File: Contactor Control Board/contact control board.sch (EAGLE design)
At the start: 35 parts, among them Q1 2n2222, Q2 2n2222, Q3 2n2222, Q4 MOSFET-NCHANNELFQP30N06L

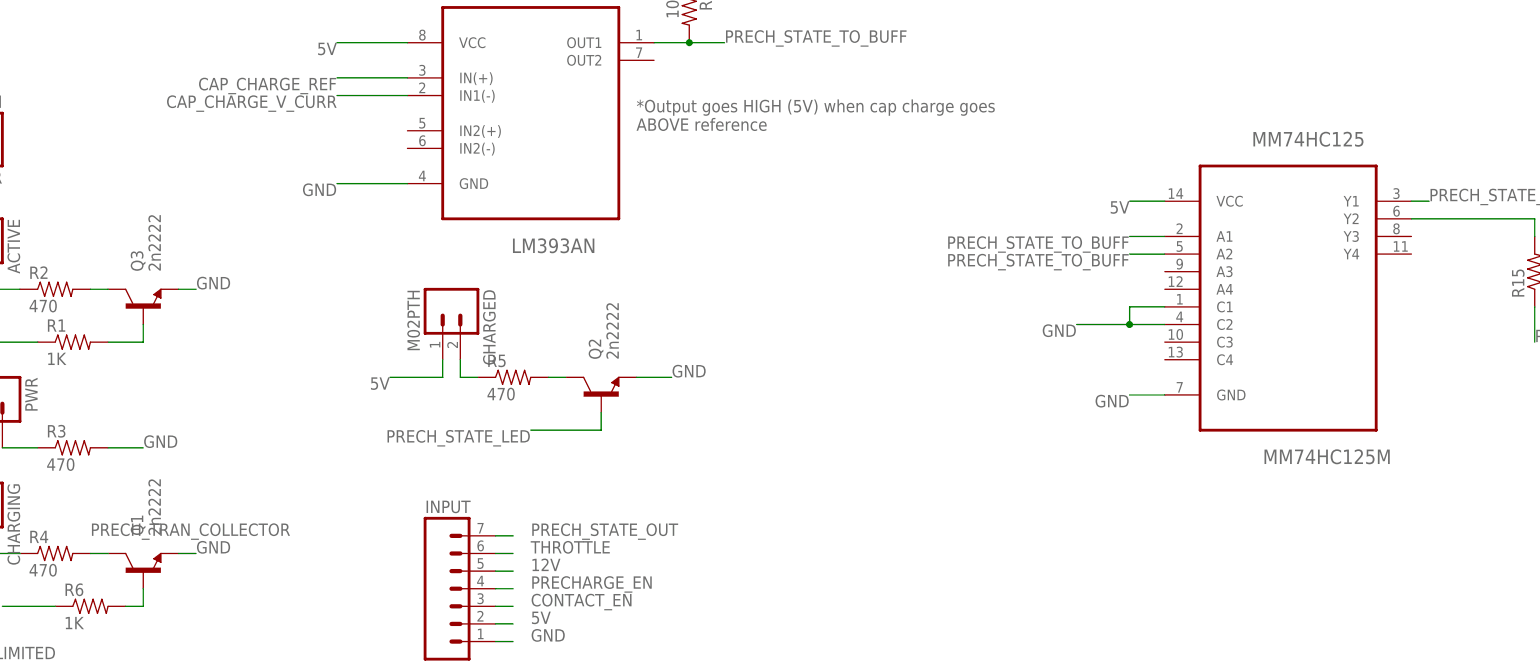
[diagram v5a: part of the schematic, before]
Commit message: Using the proper chip package for the buffer chip
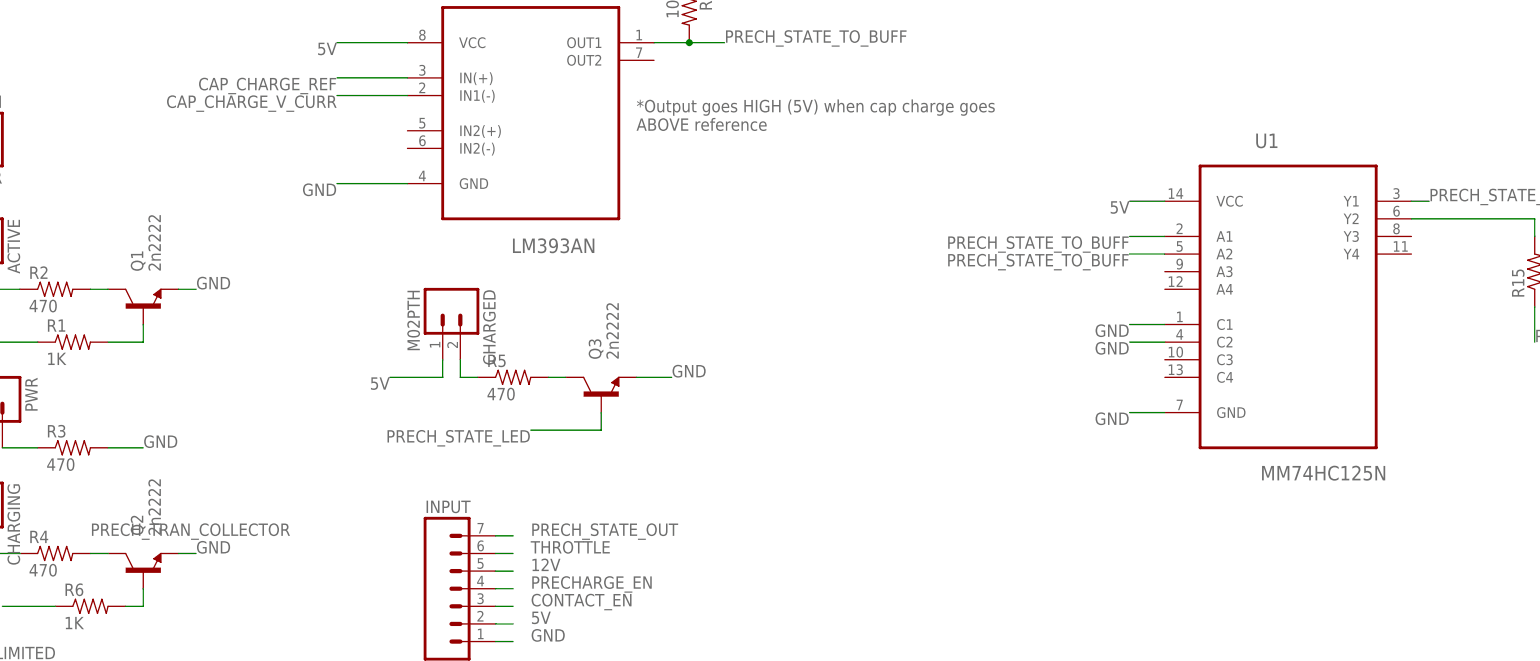
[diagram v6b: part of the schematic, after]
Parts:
- removed MM74HC125: MM74HC125M, Fairchild_By_element14_Batch_1:MM74HC125M
- added U1: MM74HC125N, mm74hc125n:MM74HC125N
- Q1, Q2, Q3: device SparkFun-DiscreteSemi:TRANSISTOR_NPNTO92 -> SparkFun-DiscreteSemi:TRANSISTOR_NPNTO-92-AMMO
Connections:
- net 5V: now also U1.VCC; no longer MM74HC125.VCC
- net GND: now also U1.C1, U1.C2, U1.GND; no longer MM74HC125.C1, MM74HC125.C2, MM74HC125.GND
- net N$1: now also Q1.C; no longer Q3.C
- net N$2: now also Q1.B; no longer Q3.B
- net N$5: now also Q3.C; no longer Q2.C
- net N$6: now also U1.Y2; no longer MM74HC125.Y2
- net PRECH_STATE_LED: now also Q3.B; no longer Q2.B
- net PRECH_STATE_OUT: now also U1.Y1; no longer MM74HC125.Y1
- net PRECH_STATE_TO_BUFF: now also U1.A1, U1.A2; no longer MM74HC125.A1, MM74HC125.A2
- net PRECH_TRAN_COLLECTOR: now also Q2.C; no longer Q1.C
- net PRECH_TRAN_IN: now also Q2.B; no longer Q1.B
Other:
- moved on the sheet: Q1, Q2, Q3
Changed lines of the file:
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@@
 <part name="PWR" library="SparkFun-Connectors" deviceset="M02" device="PTH"/>
 <part name="CHARGING" library="SparkFun-Connectors" deviceset="M02" device="PTH"/>
-<part name="Q1" library="SparkFun-DiscreteSemi" deviceset="TRANSISTOR_NPN" device="TO92" value="2n2222"/>
-<part name="Q3" library="SparkFun-DiscreteSemi" deviceset="TRANSISTOR_NPN" device="TO92" value="2n2222"/>
 <part name="RESISTOR" library="SparkFun-Connectors" deviceset="M02" device="2.54MM_SCREWTERM"/>
 <part name="R8" library="SparkFun-Resistors" deviceset="RESISTOR" device="PTH-1/4W" value="470k"/>
@@
 <part name="INPUT" library="SparkFun-Connectors" deviceset="M07" device=""/>
 <part name="CHARGED" library="SparkFun-Connectors" deviceset="M02" device="PTH"/>
-<part name="Q2" library="SparkFun-DiscreteSemi" deviceset="TRANSISTOR_NPN" device="TO92" value="2n2222"/>
 <part name="R5" library="SparkFun-Resistors" deviceset="RESISTOR" device="PTH-1/4W" value="470"/>
 <part name="R14" library="SparkFun-Resistors" deviceset="RESISTOR" device="PTH-1/4W" value="10K"/>
-<part name="MM74HC125" library="Fairchild_By_element14_Batch_1" deviceset="MM74HC125M" device=""/>
 <part name="R15" library="SparkFun-Resistors" deviceset="RESISTOR" device="PTH-1/4W" value="1k"/>
+<part name="U1" library="mm74hc125n" deviceset="MM74HC125N" device=""/>
+<part name="Q3" library="SparkFun-DiscreteSemi" deviceset="TRANSISTOR_NPN" device="TO-92-AMMO" value="2n2222"/>
+<part name="Q1" library="SparkFun-DiscreteSemi" deviceset="TRANSISTOR_NPN" device="TO-92-AMMO" value="2n2222"/>
+<part name="Q2" library="SparkFun-DiscreteSemi" deviceset="TRANSISTOR_NPN" device="TO-92-AMMO" value="2n2222"/>
 </parts>
 <sheets>
@@
 <instance part="PWR" gate="G$1" x="53.34" y="76.2" rot="R270"/>
 <instance part="CHARGING" gate="G$1" x="50.8" y="60.96" rot="R270"/>
-<instance part="Q1" gate="G$1" x="76.2" y="50.8" rot="R90"/>
-<instance part="Q3" gate="G$1" x="76.2" y="88.9" rot="R90"/>
 <instance part="RESISTOR" gate="G$1" x="53.34" y="114.3" rot="R180"/>
 <instance part="R8" gate="G$1" x="71.12" y="160.02" rot="R270"/>
@@
 <instance part="INPUT" gate="G$1" x="121.92" y="45.72"/>
 <instance part="CHARGED" gate="G$1" x="119.38" y="88.9" rot="R270"/>
-<instance part="Q2" gate="G$1" x="142.24" y="76.2" rot="R90"/>
 <instance part="R5" gate="G$1" x="129.54" y="78.74"/>
 <instance part="R14" gate="G$1" x="20.32" y="38.1" rot="R180"/>
-<instance part="MM74HC125" gate="A" x="241.3" y="93.98"/>
 <instance part="R15" gate="G$1" x="276.86" y="93.98" rot="R90"/>
+<instance part="U1" gate="A" x="241.3" y="91.44"/>
+<instance part="Q3" gate="G$1" x="142.24" y="76.2" rot="R90"/>
+<instance part="Q1" gate="G$1" x="76.2" y="88.9" rot="R90"/>
+<instance part="Q2" gate="G$1" x="76.2" y="50.8" rot="R90"/>
 </instances>
 <busses>
@@
 </segment>
 <segment>
-<pinref part="MM74HC125" gate="A" pin="VCC"/>
 <wire x1="223.52" y1="104.14" x2="218.44" y2="104.14" width="0.2032" layer="91"/>
 <label x="218.44" y="104.14" size="1.778" layer="95" rot="R180"/>
+<pinref part="U1" gate="A" pin="VCC"/>
 </segment>
 </net>
@@
 </segment>
 <segment>
-<pinref part="Q1" gate="G$1" pin="E"/>
 <wire x1="81.28" y1="53.34" x2="83.82" y2="53.34" width="0.2032" layer="91"/>
 <label x="83.82" y="53.34" size="1.778" layer="95"/>
-</segment>
-<segment>
-<pinref part="Q3" gate="G$1" pin="E"/>
+<pinref part="Q2" gate="G$1" pin="E"/>
+</segment>
+<segment>
 <wire x1="81.28" y1="91.44" x2="83.82" y2="91.44" width="0.2032" layer="91"/>
 <label x="83.82" y="91.44" size="1.778" layer="95"/>
+<pinref part="Q1" gate="G$1" pin="E"/>
 </segment>
 <segment>
@@
 </segment>
 <segment>
-<pinref part="Q2" gate="G$1" pin="E"/>
 <wire x1="147.32" y1="78.74" x2="152.4" y2="78.74" width="0.2032" layer="91"/>
 <label x="152.4" y="78.74" size="1.778" layer="95"/>
+<pinref part="Q3" gate="G$1" pin="E"/>
 </segment>
 <segment>
@@
 </segment>
 <segment>
-<pinref part="MM74HC125" gate="A" pin="GND"/>
-<wire x1="223.52" y1="76.2" x2="218.44" y2="76.2" width="0.2032" layer="91"/>
-<label x="218.44" y="76.2" size="1.778" layer="95" rot="R180"/>
-</segment>
-<segment>
-<pinref part="MM74HC125" gate="A" pin="C1"/>
-<wire x1="223.52" y1="88.9" x2="218.44" y2="88.9" width="0.2032" layer="91"/>
-<wire x1="218.44" y1="88.9" x2="218.44" y2="86.36" width="0.2032" layer="91"/>
-<wire x1="218.44" y1="86.36" x2="210.82" y2="86.36" width="0.2032" layer="91"/>
-<pinref part="MM74HC125" gate="A" pin="C2"/>
+<pinref part="U1" gate="A" pin="C1"/>
 <wire x1="223.52" y1="86.36" x2="218.44" y2="86.36" width="0.2032" layer="91"/>
-<junction x="218.44" y="86.36"/>
-<label x="210.82" y="86.36" size="1.778" layer="95" rot="R180"/>
+<label x="218.44" y="86.36" size="1.778" layer="95" rot="R180"/>
+</segment>
+<segment>
+<pinref part="U1" gate="A" pin="C2"/>
+<wire x1="223.52" y1="83.82" x2="218.44" y2="83.82" width="0.2032" layer="91"/>
+<label x="218.44" y="83.82" size="1.778" layer="95" rot="R180"/>
+</segment>
+<segment>
+<pinref part="U1" gate="A" pin="GND"/>
+<wire x1="223.52" y1="73.66" x2="218.44" y2="73.66" width="0.2032" layer="91"/>
+<label x="218.44" y="73.66" size="1.778" layer="95" rot="R180"/>
 </segment>
 </net>
@@
 <pinref part="R2" gate="G$1" pin="2"/>
 <wire x1="71.12" y1="91.44" x2="68.58" y2="91.44" width="0.1524" layer="91"/>
-<pinref part="Q3" gate="G$1" pin="C"/>
+<pinref part="Q1" gate="G$1" pin="C"/>
 </segment>
 </net>
@@
 <wire x1="71.12" y1="53.34" x2="68.58" y2="53.34" width="0.1524" layer="91"/>
 <label x="68.58" y="55.88" size="1.778" layer="95"/>
-<pinref part="Q1" gate="G$1" pin="C"/>
+<pinref part="Q2" gate="G$1" pin="C"/>
 </segment>
 <segment>
@@
 </segment>
 <segment>
-<pinref part="MM74HC125" gate="A" pin="Y1"/>
 <wire x1="259.08" y1="104.14" x2="261.62" y2="104.14" width="0.2032" layer="91"/>
 <label x="261.62" y="104.14" size="1.778" layer="95"/>
+<pinref part="U1" gate="A" pin="Y1"/>
 </segment>
 </net>
@@
 <segment>
 <pinref part="R1" gate="G$1" pin="2"/>
-<pinref part="Q3" gate="G$1" pin="B"/>
 <wire x1="71.12" y1="83.82" x2="76.2" y2="83.82" width="0.2032" layer="91"/>
 <wire x1="76.2" y1="83.82" x2="76.2" y2="86.36" width="0.2032" layer="91"/>
+<pinref part="Q1" gate="G$1" pin="B"/>
 </segment>
 </net>
@@
 <segment>
 <pinref part="R6" gate="G$1" pin="2"/>
-<pinref part="Q1" gate="G$1" pin="B"/>
 <wire x1="73.66" y1="45.72" x2="76.2" y2="45.72" width="0.2032" layer="91"/>
 <wire x1="76.2" y1="45.72" x2="76.2" y2="48.26" width="0.2032" layer="91"/>
+<pinref part="Q2" gate="G$1" pin="B"/>
 </segment>
 </net>
@@
 <segment>
 <pinref part="R5" gate="G$1" pin="2"/>
-<pinref part="Q2" gate="G$1" pin="C"/>
 <wire x1="134.62" y1="78.74" x2="137.16" y2="78.74" width="0.2032" layer="91"/>
+<pinref part="Q3" gate="G$1" pin="C"/>
 </segment>
 </net>
@@
 </segment>
 <segment>
-<pinref part="MM74HC125" gate="A" pin="A1"/>
 <wire x1="223.52" y1="99.06" x2="218.44" y2="99.06" width="0.2032" layer="91"/>
 <label x="218.44" y="99.06" size="1.778" layer="95" rot="R180"/>
-</segment>
-<segment>
-<pinref part="MM74HC125" gate="A" pin="A2"/>
+<pinref part="U1" gate="A" pin="A1"/>
+</segment>
+<segment>
 <wire x1="223.52" y1="96.52" x2="218.44" y2="96.52" width="0.2032" layer="91"/>
 <label x="218.44" y="96.52" size="1.778" layer="95" rot="R180"/>
+<pinref part="U1" gate="A" pin="A2"/>
 </segment>
 </net>
 <net name="PRECH_STATE_LED" class="0">
 <segment>
-<pinref part="Q2" gate="G$1" pin="B"/>
 <wire x1="142.24" y1="73.66" x2="142.24" y2="71.12" width="0.2032" layer="91"/>
 <wire x1="142.24" y1="71.12" x2="132.08" y2="71.12" width="0.2032" layer="91"/>
 <label x="132.08" y="71.12" size="1.778" layer="95" rot="R180"/>
+<pinref part="Q3" gate="G$1" pin="B"/>
 </segment>
 <segment>
@@
 <net name="N$6" class="0">
 <segment>
-<pinref part="MM74HC125" gate="A" pin="Y2"/>
 <pinref part="R15" gate="G$1" pin="2"/>
 <wire x1="259.08" y1="101.6" x2="276.86" y2="101.6" width="0.2032" layer="91"/>
 <wire x1="276.86" y1="101.6" x2="276.86" y2="99.06" width="0.2032" layer="91"/>
-</segment>
-</net>
+<pinref part="U1" gate="A" pin="Y2"/>
+</segment>
+</net>
